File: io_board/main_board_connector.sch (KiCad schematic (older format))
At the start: 2 parts

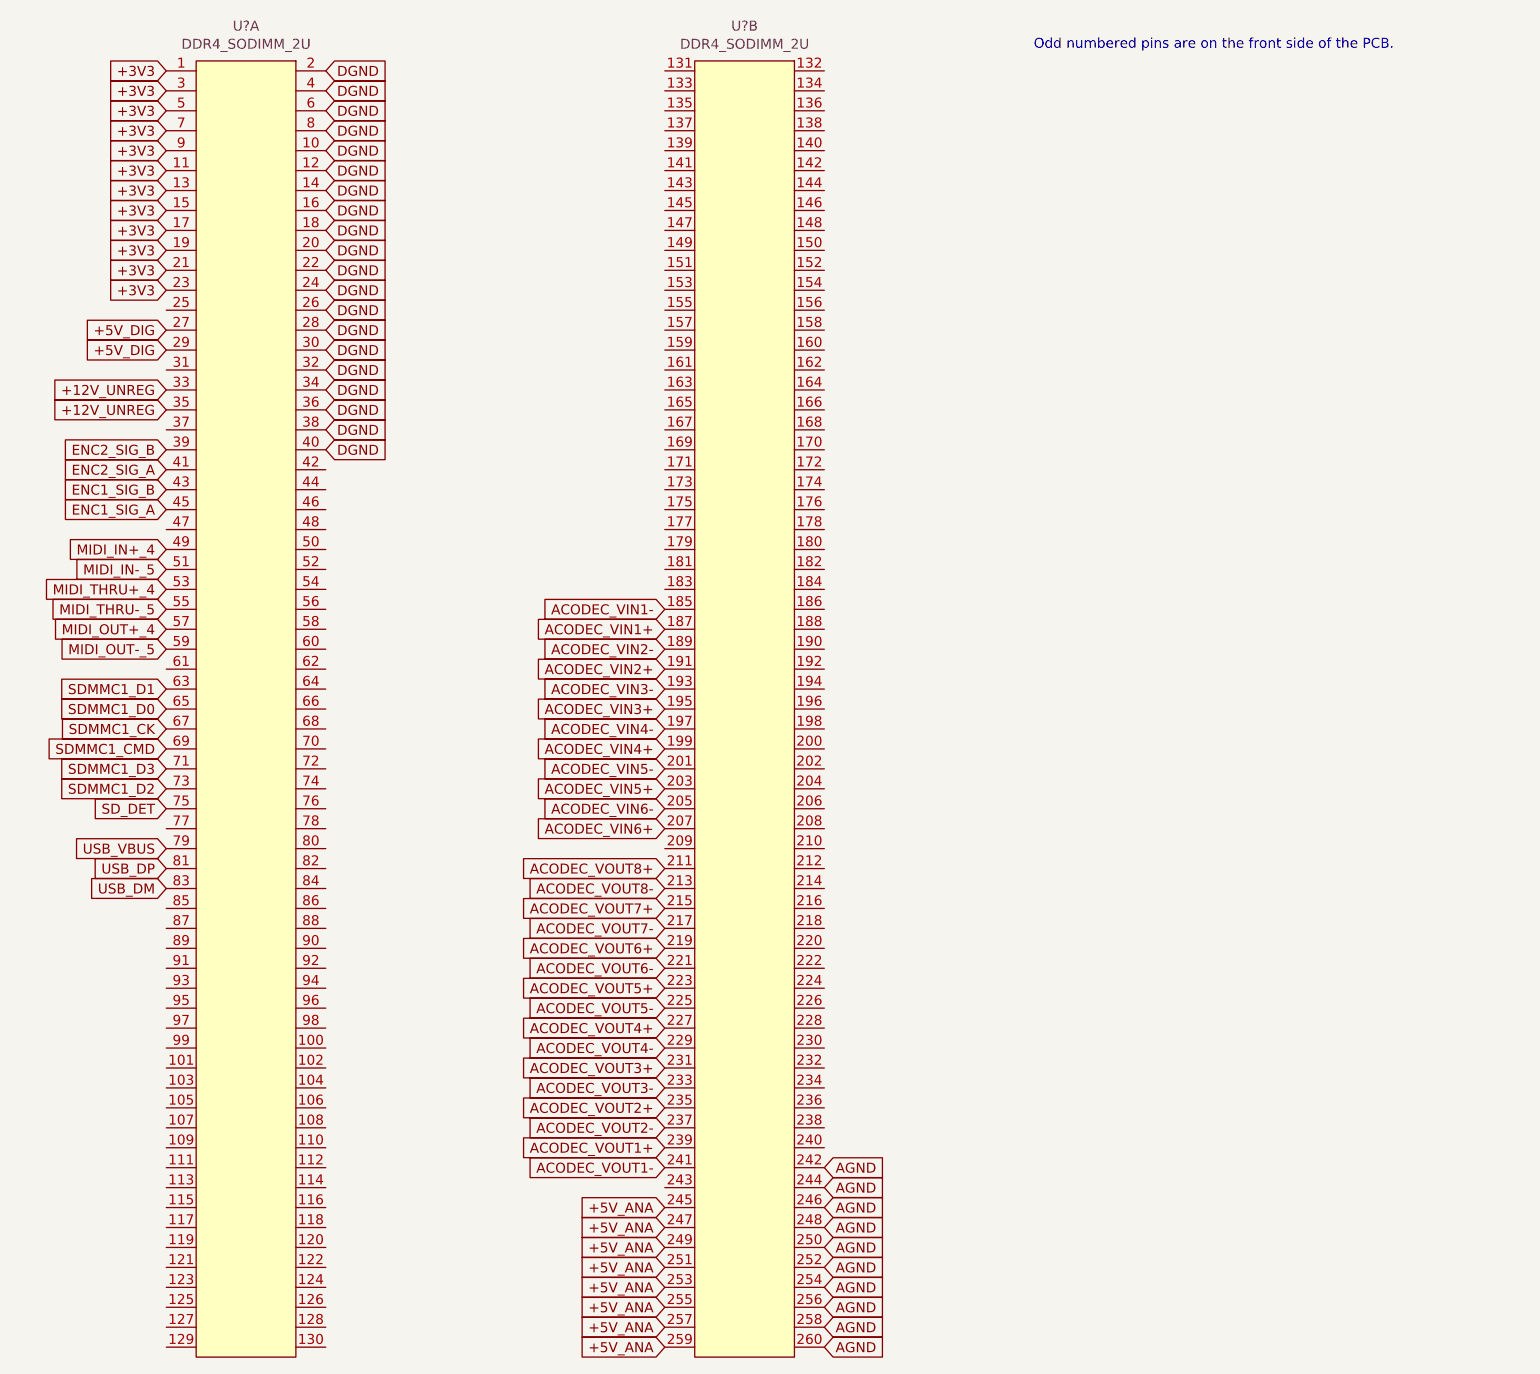
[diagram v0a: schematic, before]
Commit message: Drew input and output audio stages in the schematic
Having trouble making hierarchical sheets refering to the same schematic file.
Could be a bug but also maybe I screwed up the schematic file
io_board/main_board_connector.sch because I changed the text in it to change
some global labels into hierarchical ones.
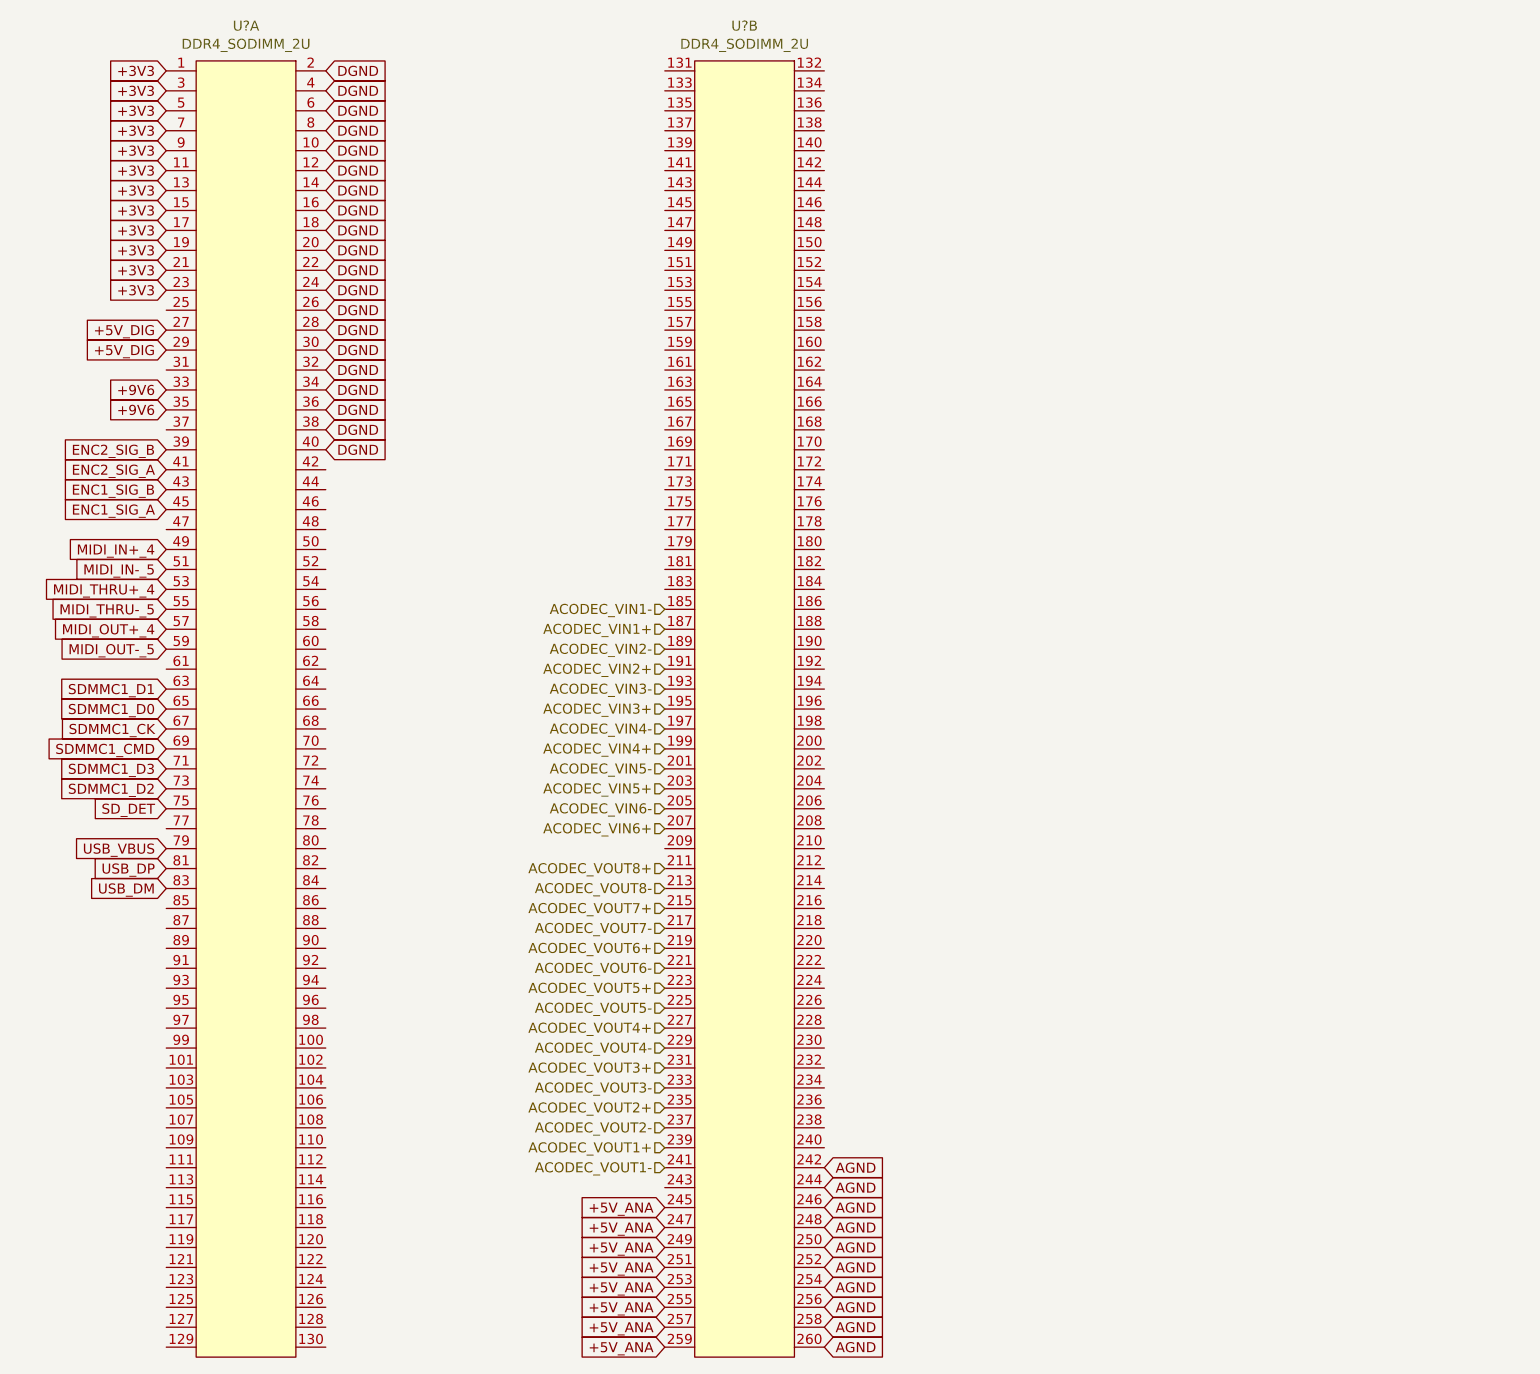
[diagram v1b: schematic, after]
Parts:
- removed U? (x2): DDR4_SODIMM_2U, symbol contrib_connectors:DDR4_SODIMM_2U
- added U? (x2): DDR4_SODIMM_2U, symbol contrib_connectors:DDR4_SODIMM_2U
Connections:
- net +3V3: now also U?.1, U?.11, U?.13, U?.15, U?.17, U?.19, U?.21, U?.23, U?.3, U?.5, U?.7, U?.9
- net +5V_ANA: now also U?.245, U?.247, U?.249, U?.251, U?.253, U?.255, U?.257, U?.259
- net +5V_DIG: now also U?.27, U?.29
- net ACODEC_VIN1+: now also U?.187
- net ACODEC_VIN1-: now also U?.185
- net ACODEC_VIN2+: now also U?.191
- net ACODEC_VIN2-: now also U?.189
- net ACODEC_VIN3+: now also U?.195
- net ACODEC_VIN3-: now also U?.193
- net ACODEC_VIN4+: now also U?.199
- net ACODEC_VIN4-: now also U?.197
- net ACODEC_VIN5+: now also U?.203
- net ACODEC_VIN5-: now also U?.201
- net ACODEC_VIN6+: now also U?.207
- net ACODEC_VIN6-: now also U?.205
- net ACODEC_VOUT1+: now also U?.239
- net ACODEC_VOUT1-: now also U?.241
- net ACODEC_VOUT2+: now also U?.235
- net ACODEC_VOUT2-: now also U?.237
- net ACODEC_VOUT3+: now also U?.231
- net ACODEC_VOUT3-: now also U?.233
- net ACODEC_VOUT4+: now also U?.227
- net ACODEC_VOUT4-: now also U?.229
- net ACODEC_VOUT5+: now also U?.223
- net ACODEC_VOUT5-: now also U?.225
- net ACODEC_VOUT6+: now also U?.219
- net ACODEC_VOUT6-: now also U?.221
- net ACODEC_VOUT7+: now also U?.215
- net ACODEC_VOUT7-: now also U?.217
- net ACODEC_VOUT8+: now also U?.211
- net ACODEC_VOUT8-: now also U?.213
- net AGND: now also U?.242, U?.244, U?.246, U?.248, U?.250, U?.252, U?.254, U?.256, U?.258, U?.260
- net DGND: now also U?.10, U?.12, U?.14, U?.16, U?.18, U?.2, U?.20, U?.22, U?.24, U?.26, U?.28, U?.30, U?.32, U?.34, U?.36, U?.38, U?.4, U?.40, U?.6, U?.8
- net ENC1_SIG_A: now also U?.45
- net ENC1_SIG_B: now also U?.43
- net ENC2_SIG_A: now also U?.41
- net ENC2_SIG_B: now also U?.39
- net MIDI_IN+_4: now also U?.49
- net MIDI_IN-_5: now also U?.51
- net MIDI_OUT+_4: now also U?.57
- net MIDI_OUT-_5: now also U?.59
- net MIDI_THRU+_4: now also U?.53
- net MIDI_THRU-_5: now also U?.55
- net SDMMC1_CK: now also U?.67
- net SDMMC1_CMD: now also U?.69
- net SDMMC1_D0: now also U?.65
- net SDMMC1_D1: now also U?.63
- net SDMMC1_D2: now also U?.73
- net SDMMC1_D3: now also U?.71
- net SD_DET: now also U?.75
- net USB_DM: now also U?.83
- net USB_DP: now also U?.81
- net USB_VBUS: now also U?.79
- new net +9V6: U?.33, U?.35
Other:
- note removed: "Odd numbered pins are on the front side of the PCB."
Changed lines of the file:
@@
 EESchema Schematic File Version 4
-LIBS:main_board-cache
+LIBS:io_board-cache
 EELAYER 26 0
 EELAYER END
 $Descr A4 11693 8268
 encoding utf-8
-Sheet 13 13
+Sheet 5 5
 Title ""
 Date ""
@@
 Comment4 ""
 $EndDescr
-$Comp
-L contrib_connectors:DDR4_SODIMM_2U U?
-U 2 1 5D07BA9D
-P 4800 4300
-F 0 "U?" V 1325 4300 50  0000 C CNN
-F 1 "DDR4_SODIMM_2U" V 1416 4300 50  0000 C CNN
-F 2 "" H 4800 4300 50  0001 C CNN
-F 3 "" H 4800 4300 50  0001 C CNN
-	2    4800 4300
-	0    1    1    0
-$EndComp
-Text Notes 6250 950  0    50   ~ 0
-Odd numbered pins are on the front side of the PCB.
 Text GLabel 1900 1050 0    50   Input ~ 0
 +3V3
@@
 +5V_DIG
 Text GLabel 1900 2650 0    50   Input ~ 0
-+12V_UNREG
++9V6
 Text GLabel 1900 2750 0    50   Input ~ 0
-+12V_UNREG
++9V6
 Text GLabel 2700 1050 2    50   Input ~ 0
 DGND
@@
 Text GLabel 4400 6750 0    50   Input ~ 0
 +5V_ANA
+Text GLabel 2700 1150 2    50   Input ~ 0
+DGND
+Text GLabel 2700 1250 2    50   Input ~ 0
+DGND
+Text GLabel 2700 1350 2    50   Input ~ 0
+DGND
+Text GLabel 2700 1450 2    50   Input ~ 0
+DGND
+Text GLabel 2700 1550 2    50   Input ~ 0
+DGND
+Text GLabel 2700 1650 2    50   Input ~ 0
+DGND
+Text GLabel 2700 1750 2    50   Input ~ 0
+DGND
+Text GLabel 2700 1850 2    50   Input ~ 0
+DGND
+Text GLabel 2700 1950 2    50   Input ~ 0
+DGND
+Text GLabel 2700 2050 2    50   Input ~ 0
+DGND
+Text GLabel 2700 2150 2    50   Input ~ 0
+DGND
+Text GLabel 2700 2250 2    50   Input ~ 0
+DGND
+Text GLabel 2700 2350 2    50   Input ~ 0
+DGND
+Text GLabel 2700 2450 2    50   Input ~ 0
+DGND
+Text GLabel 2700 2550 2    50   Input ~ 0
+DGND
+Text GLabel 2700 2650 2    50   Input ~ 0
+DGND
+Text GLabel 2700 2750 2    50   Input ~ 0
+DGND
+Text GLabel 2700 2850 2    50   Input ~ 0
+DGND
+Text GLabel 2700 2950 2    50   Input ~ 0
+DGND
+Text GLabel 5200 6550 2    50   Input ~ 0
+AGND
+Text GLabel 5200 6650 2    50   Input ~ 0
+AGND
+Text GLabel 5200 6750 2    50   Input ~ 0
+AGND
+Text GLabel 5200 6850 2    50   Input ~ 0
+AGND
+Text GLabel 5200 6950 2    50   Input ~ 0
+AGND
+Text GLabel 5200 7050 2    50   Input ~ 0
+AGND
+Text GLabel 5200 7150 2    50   Input ~ 0
+AGND
+Text GLabel 5200 7250 2    50   Input ~ 0
+AGND
+Text GLabel 5200 7350 2    50   Input ~ 0
+AGND
+Text GLabel 5200 7450 2    50   Input ~ 0
+AGND
+Text HLabel 4400 6450 0    50   Input ~ 0
+ACODEC_VOUT1+
+Text HLabel 4400 6350 0    50   Input ~ 0
+ACODEC_VOUT2-
+Text HLabel 4400 6250 0    50   Input ~ 0
+ACODEC_VOUT2+
+Text HLabel 4400 6150 0    50   Input ~ 0
+ACODEC_VOUT3-
+Text HLabel 4400 6050 0    50   Input ~ 0
+ACODEC_VOUT3+
+Text HLabel 4400 5950 0    50   Input ~ 0
+ACODEC_VOUT4-
+Text HLabel 4400 5850 0    50   Input ~ 0
+ACODEC_VOUT4+
+Text HLabel 4400 5750 0    50   Input ~ 0
+ACODEC_VOUT5-
+Text HLabel 4400 5650 0    50   Input ~ 0
+ACODEC_VOUT5+
+Text HLabel 4400 5550 0    50   Input ~ 0
+ACODEC_VOUT6-
+Text HLabel 4400 5450 0    50   Input ~ 0
+ACODEC_VOUT6+
+Text HLabel 4400 5350 0    50   Input ~ 0
+ACODEC_VOUT7-
+Text HLabel 4400 5250 0    50   Input ~ 0
+ACODEC_VOUT7+
+Text HLabel 4400 5150 0    50   Input ~ 0
+ACODEC_VOUT8-
+Text HLabel 4400 5050 0    50   Input ~ 0
+ACODEC_VOUT8+
+Text HLabel 4400 4150 0    50   Input ~ 0
+ACODEC_VIN3-
+Text HLabel 4400 4250 0    50   Input ~ 0
+ACODEC_VIN3+
+Text HLabel 4400 4350 0    50   Input ~ 0
+ACODEC_VIN4-
+Text HLabel 4400 4450 0    50   Input ~ 0
+ACODEC_VIN4+
+Text HLabel 4400 4550 0    50   Input ~ 0
+ACODEC_VIN5-
+Text HLabel 4400 4650 0    50   Input ~ 0
+ACODEC_VIN5+
+Text HLabel 4400 4750 0    50   Input ~ 0
+ACODEC_VIN6-
+Text HLabel 4400 4850 0    50   Input ~ 0
+ACODEC_VIN6+
 $Comp
 L contrib_connectors:DDR4_SODIMM_2U U?
-U 1 1 5D07B94B
+U 1 1 5D43C3EB
 P 2300 4300
 F 0 "U?" V -1175 4300 50  0000 C CNN
@@
 	0    1    1    0
 $EndComp
-Text GLabel 2700 1150 2    50   Input ~ 0
-DGND
-Text GLabel 2700 1250 2    50   Input ~ 0
-DGND
-Text GLabel 2700 1350 2    50   Input ~ 0
-DGND
-Text GLabel 2700 1450 2    50   Input ~ 0
-DGND
-Text GLabel 2700 1550 2    50   Input ~ 0
-DGND
-Text GLabel 2700 1650 2    50   Input ~ 0
-DGND
-Text GLabel 2700 1750 2    50   Input ~ 0
-DGND
-Text GLabel 2700 1850 2    50   Input ~ 0
-DGND
-Text GLabel 2700 1950 2    50   Input ~ 0
-DGND
-Text GLabel 2700 2050 2    50   Input ~ 0
-DGND
-Text GLabel 2700 2150 2    50   Input ~ 0
-DGND
-Text GLabel 2700 2250 2    50   Input ~ 0
-DGND
-Text GLabel 2700 2350 2    50   Input ~ 0
-DGND
-Text GLabel 2700 2450 2    50   Input ~ 0
-DGND
-Text GLabel 2700 2550 2    50   Input ~ 0
-DGND
-Text GLabel 2700 2650 2    50   Input ~ 0
-DGND
-Text GLabel 2700 2750 2    50   Input ~ 0
-DGND
-Text GLabel 2700 2850 2    50   Input ~ 0
-DGND
-Text GLabel 2700 2950 2    50   Input ~ 0
-DGND
-Text GLabel 5200 6550 2    50   Input ~ 0
-AGND
-Text GLabel 5200 6650 2    50   Input ~ 0
-AGND
-Text GLabel 5200 6750 2    50   Input ~ 0
-AGND
-Text GLabel 5200 6850 2    50   Input ~ 0
-AGND
-Text GLabel 5200 6950 2    50   Input ~ 0
-AGND
-Text GLabel 5200 7050 2    50   Input ~ 0
-AGND
-Text GLabel 5200 7150 2    50   Input ~ 0
-AGND
-Text GLabel 5200 7250 2    50   Input ~ 0
-AGND
-Text GLabel 5200 7350 2    50   Input ~ 0
-AGND
-Text GLabel 5200 7450 2    50   Input ~ 0
-AGND
-Text GLabel 4400 6550 0    50   Input ~ 0
+$Comp
+L contrib_connectors:DDR4_SODIMM_2U U?
+U 2 1 5D43C569
+P 4800 4300
+F 0 "U?" V 1325 4300 50  0000 C CNN
+F 1 "DDR4_SODIMM_2U" V 1416 4300 50  0000 C CNN
+F 2 "" H 4800 4300 50  0001 C CNN
+F 3 "" H 4800 4300 50  0001 C CNN
+	2    4800 4300
+	0    1    1    0
+$EndComp
+Text HLabel 4400 3750 0    50   Input ~ 0
+ACODEC_VIN1-
+Text HLabel 4400 3850 0    50   Input ~ 0
+ACODEC_VIN1+
+Text HLabel 4400 3950 0    50   Input ~ 0
+ACODEC_VIN2-
+Text HLabel 4400 4050 0    50   Input ~ 0
+ACODEC_VIN2+
+Text HLabel 4400 6550 0    50   Input ~ 0
 ACODEC_VOUT1-
-Text GLabel 4400 6450 0    50   Input ~ 0
-ACODEC_VOUT1+
-Text GLabel 4400 6350 0    50   Input ~ 0
-ACODEC_VOUT2-
-Text GLabel 4400 6250 0    50   Input ~ 0
-ACODEC_VOUT2+
-Text GLabel 4400 6150 0    50   Input ~ 0
-ACODEC_VOUT3-
-Text GLabel 4400 6050 0    50   Input ~ 0
-ACODEC_VOUT3+
-Text GLabel 4400 5950 0    50   Input ~ 0
-ACODEC_VOUT4-
-Text GLabel 4400 5850 0    50   Input ~ 0
-ACODEC_VOUT4+
-Text GLabel 4400 5750 0    50   Input ~ 0
-ACODEC_VOUT5-
-Text GLabel 4400 5650 0    50   Input ~ 0
-ACODEC_VOUT5+
-Text GLabel 4400 5550 0    50   Input ~ 0
-ACODEC_VOUT6-
-Text GLabel 4400 5450 0    50   Input ~ 0
-ACODEC_VOUT6+
-Text GLabel 4400 5350 0    50   Input ~ 0
-ACODEC_VOUT7-
-Text GLabel 4400 5250 0    50   Input ~ 0
-ACODEC_VOUT7+
-Text GLabel 4400 5150 0    50   Input ~ 0
-ACODEC_VOUT8-
-Text GLabel 4400 5050 0    50   Input ~ 0
-ACODEC_VOUT8+
-Text GLabel 4400 3750 0    50   Input ~ 0
-ACODEC_VIN1-
-Text GLabel 4400 3850 0    50   Input ~ 0
-ACODEC_VIN1+
-Text GLabel 4400 3950 0    50   Input ~ 0
-ACODEC_VIN2-
-Text GLabel 4400 4050 0    50   Input ~ 0
-ACODEC_VIN2+
-Text GLabel 4400 4150 0    50   Input ~ 0
-ACODEC_VIN3-
-Text GLabel 4400 4250 0    50   Input ~ 0
-ACODEC_VIN3+
-Text GLabel 4400 4350 0    50   Input ~ 0
-ACODEC_VIN4-
-Text GLabel 4400 4450 0    50   Input ~ 0
-ACODEC_VIN4+
-Text GLabel 4400 4550 0    50   Input ~ 0
-ACODEC_VIN5-
-Text GLabel 4400 4650 0    50   Input ~ 0
-ACODEC_VIN5+
-Text GLabel 4400 4750 0    50   Input ~ 0
-ACODEC_VIN6-
-Text GLabel 4400 4850 0    50   Input ~ 0
-ACODEC_VIN6+
 $EndSCHEMATC
